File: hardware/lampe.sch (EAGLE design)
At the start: 30 parts, among them IC1 ATMEGA168-20P, IC3 DS1307, Q2 16Mhz, Q3 32.768kHz, Q4 BUZ11BV, T3 BC547B, T4 BC547B, X1 MKDSN1,5/2-5,08, X2 MKDSN1,5/2-5,08

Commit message: Minors.
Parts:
- added R1: 1k, rcl:R-EU_0204/2V
- added R2: 10k, ptc-ntc:B57164
- R27: value 10k -> 6.1k
- R28: value 10k -> 1k
- R29: value 1k -> 10k
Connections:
- new net N$10: IC1.(PCI8/ADC0)PC0, R1.1, R2.1
- net +5V: now also R2.2
- net GND: now also R1.2
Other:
- note added: "2.0-3.5V"
- note added: "R = 0.6/Imax"
- note removed: "3V"
- note removed: "Rges = 0.65/Imax"
- moved on the sheet: C1, C10, C9, G1, IC3, JP1, KK1, Q3, Q4, R12, R13, R24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

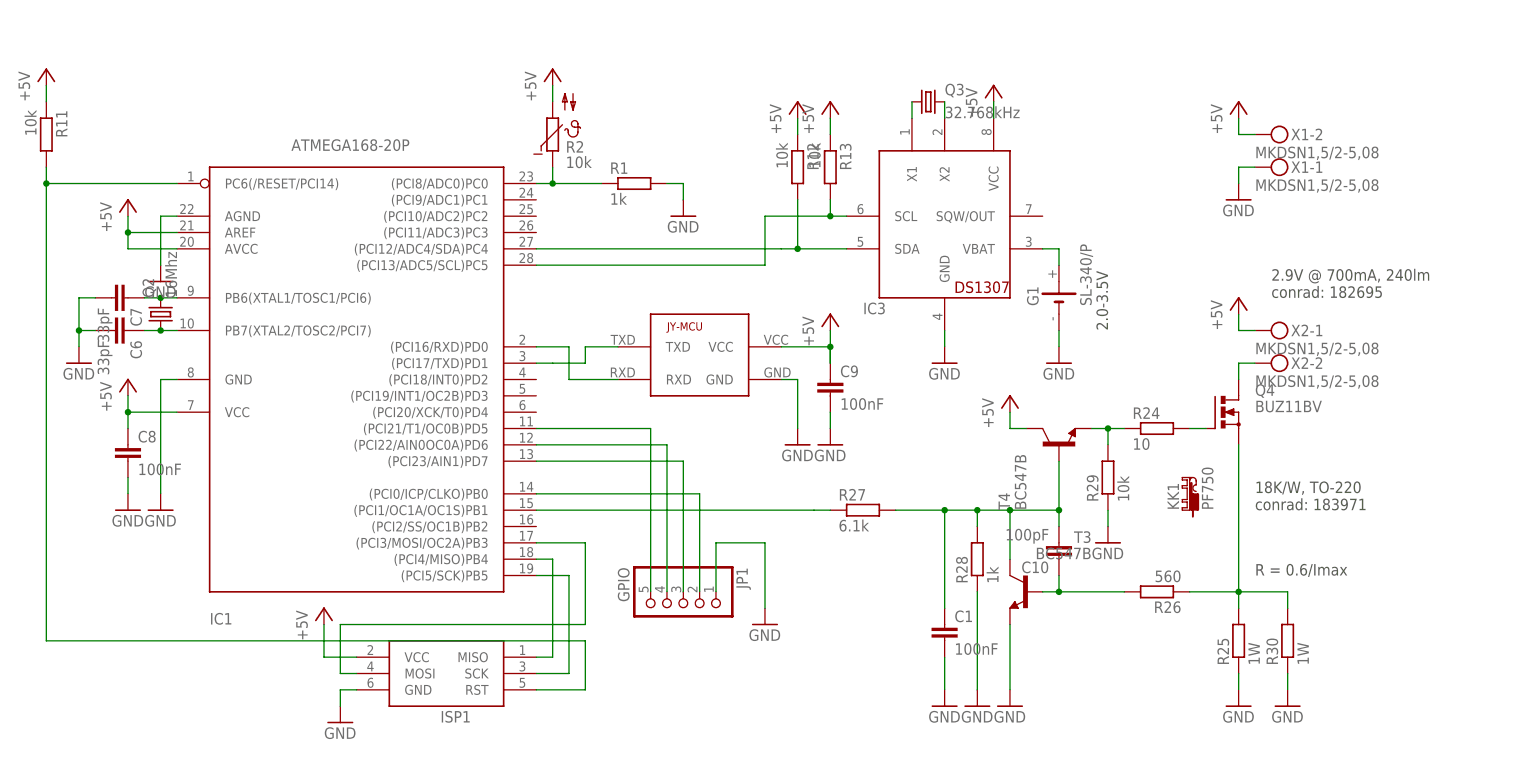
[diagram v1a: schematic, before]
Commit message: Fixed current reg.
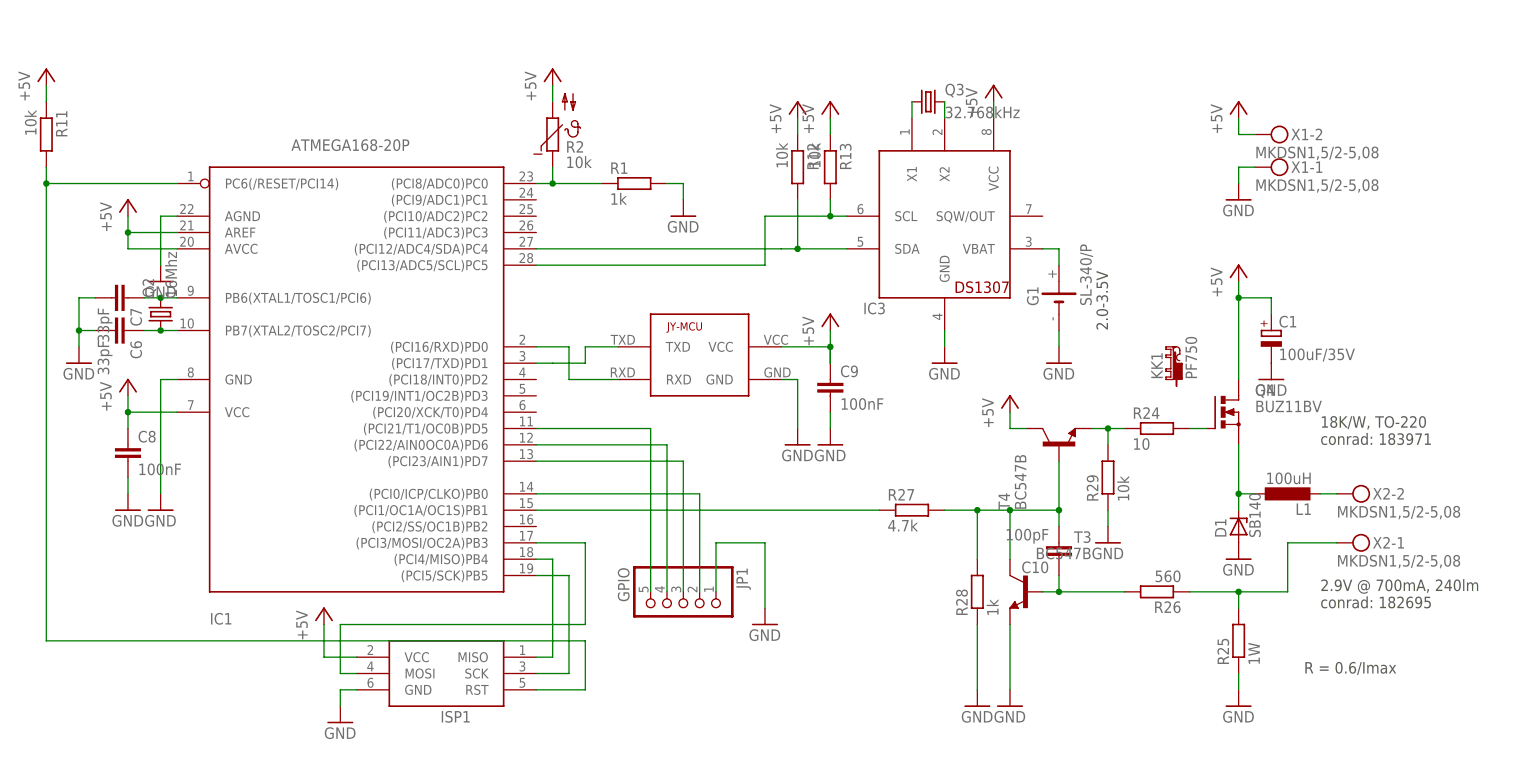
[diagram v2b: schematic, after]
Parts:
- removed R30: 1W, rcl:R-EU_0411/12
- added D1: SB140, diode:ZENER-DIODEDO35Z10
- added L1: 100uH, rcl:L-EU6000-XXX-RC
- C1: value 100nF -> 100uF/35V; device rcl:C-EU050-025X075 -> rcl:CPOL-EUE5-6
- R26: device rcl:R-EU_0204/7 -> rcl:R-EU_0207/17
- R27: value 6.1k -> 4.7k
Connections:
- removed net N$38: Q4.D, X2-2.KL
- new net N$11: D1.C, L1.1, Q4.S
- new net N$15: L1.2, X2-2.KL
- net +5V: now also C1.+, Q4.D; no longer X2-1.KL
- net GND: now also C1.-, D1.A; no longer C1.2, R30.1
- net N$39: now also X2-1.KL; no longer Q4.S, R30.2
- net N$41: no longer C1.1
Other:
- moved on the sheet: KK1, R27, R28, X2-1, X2-2

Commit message: Updated circuit and board PDFs.
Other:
- moved on the sheet: C1, KK1, X1-1, X1-2, X2-1
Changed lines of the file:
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@@
 <?xml version="1.0" encoding="utf-8"?>
 <!DOCTYPE eagle SYSTEM "eagle.dtd">
-<eagle version="7.1.0">
+<eagle version="7.2.0">
 <drawing>
 <settings>
@@
 <sheet>
 <plain>
-<text x="142.24" y="-68.58" size="1.778" layer="97">2.9V @ 700mA, 240lm
+<text x="139.7" y="-63.5" size="1.778" layer="97">2.9V @ 700mA, 240lm
 conrad: 182695</text>
-<text x="142.24" y="-43.18" size="1.778" layer="97">18K/W, TO-220
+<text x="111.76" y="-27.94" size="1.778" layer="97">18K/W, TO-220
 conrad: 183971</text>
 <text x="109.22" y="-25.4" size="1.778" layer="97" rot="R90">2.0-3.5V</text>
-<text x="139.7" y="-78.74" size="1.778" layer="97">R = 0.6/Imax</text>
+<text x="132.08" y="-81.28" size="1.778" layer="97">R = 0.6/Imax</text>
 </plain>
 <instances>
@@
 <instance part="GND18" gate="1" x="60.96" y="-43.18"/>
 <instance part="GND19" gate="1" x="66.04" y="-43.18"/>
-<instance part="P+12" gate="1" x="129.54" y="10.16"/>
-<instance part="GND20" gate="1" x="129.54" y="-5.08"/>
+<instance part="P+12" gate="1" x="144.78" y="12.7"/>
+<instance part="GND20" gate="1" x="144.78" y="-2.54"/>
 <instance part="R24" gate="G$1" x="116.84" y="-40.64"/>
 <instance part="Q4" gate="1" x="127" y="-38.1"/>
@@
 <instance part="GND27" gate="1" x="109.22" y="-58.42"/>
 <instance part="P+1" gate="1" x="93.98" y="-35.56"/>
-<instance part="P+2" gate="1" x="129.54" y="-15.24"/>
-<instance part="X1" gate="-1" x="134.62" y="0"/>
-<instance part="X1" gate="-2" x="134.62" y="5.08"/>
-<instance part="X2" gate="-1" x="147.32" y="-58.42"/>
+<instance part="P+2" gate="1" x="129.54" y="-12.7"/>
+<instance part="X1" gate="-1" x="149.86" y="2.54"/>
+<instance part="X1" gate="-2" x="149.86" y="7.62"/>
+<instance part="X2" gate="-1" x="147.32" y="-66.04"/>
 <instance part="X2" gate="-2" x="147.32" y="-50.8"/>
 <instance part="IC1" gate="G$1" x="-12.7" y="-30.48"/>
@@
 <instance part="JP1" gate="A" x="43.18" y="-68.58" rot="R270"/>
 <instance part="GND5" gate="1" x="55.88" y="-71.12"/>
-<instance part="KK1" gate="G$1" x="119.38" y="-30.48"/>
+<instance part="KK1" gate="G$1" x="121.92" y="-33.02"/>
 <instance part="R1" gate="G$1" x="35.56" y="-2.54"/>
 <instance part="R2" gate="1" x="22.86" y="5.08"/>
@@
 <instance part="GND6" gate="1" x="43.18" y="-7.62"/>
 <instance part="L1" gate="G$1" x="137.16" y="-50.8" rot="R90"/>
-<instance part="C1" gate="G$1" x="134.62" y="-25.4"/>
+<instance part="C1" gate="G$1" x="134.62" y="-22.86"/>
 <instance part="D1" gate="G$1" x="129.54" y="-55.88" rot="R90"/>
-<instance part="GND1" gate="1" x="134.62" y="-33.02"/>
+<instance part="GND1" gate="1" x="134.62" y="-30.48"/>
 <instance part="GND8" gate="1" x="129.54" y="-60.96"/>
 </instances>
@@
 <segment>
 <pinref part="P+12" gate="1" pin="+5V"/>
-<wire x1="129.54" y1="5.08" x2="129.54" y2="7.62" width="0.1524" layer="91"/>
+<wire x1="144.78" y1="7.62" x2="144.78" y2="10.16" width="0.1524" layer="91"/>
 <pinref part="X1" gate="-2" pin="KL"/>
-<wire x1="132.08" y1="5.08" x2="129.54" y2="5.08" width="0.1524" layer="91"/>
+<wire x1="147.32" y1="7.62" x2="144.78" y2="7.62" width="0.1524" layer="91"/>
 </segment>
 <segment>
@@
 <pinref part="P+2" gate="1" pin="+5V"/>
 <pinref part="Q4" gate="1" pin="D"/>
-<wire x1="129.54" y1="-17.78" x2="129.54" y2="-20.32" width="0.1524" layer="91"/>
-<wire x1="129.54" y1="-20.32" x2="129.54" y2="-33.02" width="0.1524" layer="91"/>
-<wire x1="129.54" y1="-20.32" x2="134.62" y2="-20.32" width="0.1524" layer="91"/>
+<wire x1="129.54" y1="-15.24" x2="129.54" y2="-17.78" width="0.1524" layer="91"/>
+<wire x1="129.54" y1="-17.78" x2="129.54" y2="-33.02" width="0.1524" layer="91"/>
+<wire x1="129.54" y1="-17.78" x2="134.62" y2="-17.78" width="0.1524" layer="91"/>
 <pinref part="C1" gate="G$1" pin="+"/>
-<wire x1="134.62" y1="-20.32" x2="134.62" y2="-22.86" width="0.1524" layer="91"/>
-<junction x="129.54" y="-20.32"/>
+<wire x1="134.62" y1="-17.78" x2="134.62" y2="-20.32" width="0.1524" layer="91"/>
+<junction x="129.54" y="-17.78"/>
 </segment>
 </net>
@@
 <segment>
 <pinref part="GND20" gate="1" pin="GND"/>
-<wire x1="129.54" y1="0" x2="129.54" y2="-2.54" width="0.1524" layer="91"/>
+<wire x1="144.78" y1="2.54" x2="144.78" y2="0" width="0.1524" layer="91"/>
 <pinref part="X1" gate="-1" pin="KL"/>
-<wire x1="132.08" y1="0" x2="129.54" y2="0" width="0.1524" layer="91"/>
+<wire x1="147.32" y1="2.54" x2="144.78" y2="2.54" width="0.1524" layer="91"/>
 </segment>
 <segment>
@@
 <wire x1="121.92" y1="-66.04" x2="129.54" y2="-66.04" width="0.1524" layer="91"/>
 <junction x="129.54" y="-66.04"/>
-<wire x1="129.54" y1="-66.04" x2="137.16" y2="-66.04" width="0.1524" layer="91"/>
-<wire x1="137.16" y1="-58.42" x2="137.16" y2="-66.04" width="0.1524" layer="91"/>
+<wire x1="129.54" y1="-66.04" x2="144.78" y2="-66.04" width="0.1524" layer="91"/>
 <pinref part="X2" gate="-1" pin="KL"/>
-<wire x1="144.78" y1="-58.42" x2="137.16" y2="-58.42" width="0.1524" layer="91"/>
-</segment>
-</net>
+</segment>
+</net>
